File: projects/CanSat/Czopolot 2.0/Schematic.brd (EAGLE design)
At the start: 43 x 30.8 mm, 91 parts

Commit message: Work work..
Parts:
- removed U$13: DRV8833SOP, SobieskiSat2:SOP65P640X120-17T340X500N
- added C26: 10u, Unified:C0603
- added C27, C33: 100n, Unified:C0603
- added R18, R19: 100k, Unified:R0603
- added U$14, U$15: DRV8838, SobieskiSat2:SON50P200X200X80-9T90X160N
- BTN_DFU: value PUSH-SWITCH -> PUSH-SWITCHDIP; device SobieskiSat2:SWITCH_SMD -> SobieskiSat2:2X1_2.54
- C17: value 10u_pol -> 100n; device Unified:C1206 -> Unified:C0603
- C24: value 100n -> 10u
- C25: value 2.2u -> 100n
- R12: value 10k -> 100k
- moved D7 50.7 mm to (39.2, 25.8), turned to 90 degrees
- moved D8 48.4 mm to (39.2, 23.8), turned to 90 degrees
- moved D10 47.3 mm to (39.2, 17.8)
- moved D6 45.8 mm to (39.2, 27.8)
- moved R30 42.7 mm to (39.2, 16.0), turned to 180 degrees
- moved D2 41.7 mm to (39.2, 19.8)
- moved C21 41.0 mm to (8.25, 27.2), turned to 270 degrees
- moved D9 40.7 mm to (39.2, 21.8)
- moved R10 39.9 mm to (17.5, 28.0), turned to 90 degrees
- moved C23 39.8 mm to (9.50, 30.0), turned to 0 degrees
- moved C22 39.6 mm to (10.5, 27.2), turned to 90 degrees
- moved U$9 37.7 mm to (14.0, 28.2), turned to 90 degrees
- moved R14 34.8 mm to (25.5, 11.0)
- moved R15 33.3 mm to (21.0, 7.50), turned to 90 degrees
- moved D61 33.3 mm to (14.5, 3.75)
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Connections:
- removed net AIN1: U$13.16
- removed net AIN2: U$13.15
- removed net BIN1: U$13.9
- removed net BIN2: U$13.10
- removed net N$51: D10.A, R30.2
- new net EN_L: U$1.15, U$14.5
- new net EN_R: U$1.17, U$15.5
- new net N$32: D10.C, R30.1
- new net N$33: D61.1, R63.1, U$3.P$10
- new net N$34: MOTR.P$2, U$15.2
- new net N$36: MOTR.P$1, U$15.3
- new net N$39: C17.2, C24.2, U$15.8
- new net N$40: R19.1, U$15.7
- new net PH_L: U$1.14, U$14.6
- new net PH_R: U$1.16, U$15.6
- net DFU: no longer BTN_DFU.P$3
- net GND: now also C17.1, C24.1, C26.1, C27.1, C33.1, R30.2, U$14.4, U$14.9, U$15.4, U$15.9; no longer D10.C, U$13.13, U$13.17
- net GPS_RX: now also D61.2, U$1.29; no longer U$1.42, U$3.P$10
- net GPS_TX: now also R12.2, U$1.30; no longer R31.2, U$1.43
- net N$10: now also R5.1, U$10.7; no longer MOTL.P$2, U$13.2
- net N$15: now also RN1.1, U$1.38; no longer MOTR.P$1, U$13.5
- net N$19: now also RN1.2, U$1.37; no longer C17.1, C24.1, U$13.11
- net N$20: now also RN1.3, U$1.36; no longer D2.C, U$10.7
- net N$26: now also MOTL.P$1, U$14.3; no longer C25.2, U$13.14
- net N$28: now also RN1.4, U$1.35; no longer D2.A, R5.1
- net N$29: now also R31.2, U$1.43; no longer U$13.3
- net N$3: now also D2.C, R5.2; no longer MOTR.P$2, U$13.7
- net N$30: now also C25.2, C26.2, U$14.8; no longer U$13.6
- net N$31: now also R18.1, U$14.7; no longer R12.1, U$13.1
- net N$5: now also MOTL.P$2, U$14.2; no longer MOTL.P$1, U$13.4
- net SCL: now also R6.1, U$1.58; no longer R7.2, U$1.29
- net SDA: now also R7.1, U$1.59; no longer R6.2, U$1.30
- net VCC: now also D10.A, D2.A, R12.1, R18.2, R19.2, R6.2, R63.2, R7.2; no longer BTN_DFU.P$4, R12.2, R30.1, R5.2, R6.1, R7.1
- net VSYS: now also C27.2, C33.2, U$14.1, U$15.1; no longer C17.2, C24.2, U$13.12
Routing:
- net GND: track 84.0 -> 193.7 mm, vias 0 -> 8
- net VSYS: track 0.00 -> 54.0 mm
- net SCL: track 27.1 -> 0.00 mm, vias 1 -> 0
- net SDA: track 26.6 -> 0.00 mm, vias 1 -> 0
- net N$38: track 0.00 -> 22.2 mm, vias 0 -> 1
- net N$1: track 0.00 -> 21.4 mm, vias 0 -> 1
- net N$37: track 0.00 -> 21.0 mm, vias 0 -> 1
- net VCC: track 138.4 -> 117.7 mm, vias 3 -> 4
- net N$2: track 0.00 -> 20.0 mm, vias 0 -> 1
- net N$3: track 4.08 -> 23.8 mm, vias 0 -> 1
- net GPS_TX: track 23.2 -> 8.61 mm
- net PH_L: track 0.00 -> 14.4 mm
- net EN_L: track 0.00 -> 13.8 mm
- net USB_D-: track 17.9 -> 4.37 mm
- net USB_D+: track 17.0 -> 4.10 mm
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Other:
- board size 43 x 30.8 mm -> 44.2 x 30.8 mm
- board text removed: "^ Battery and switch holes or pads"

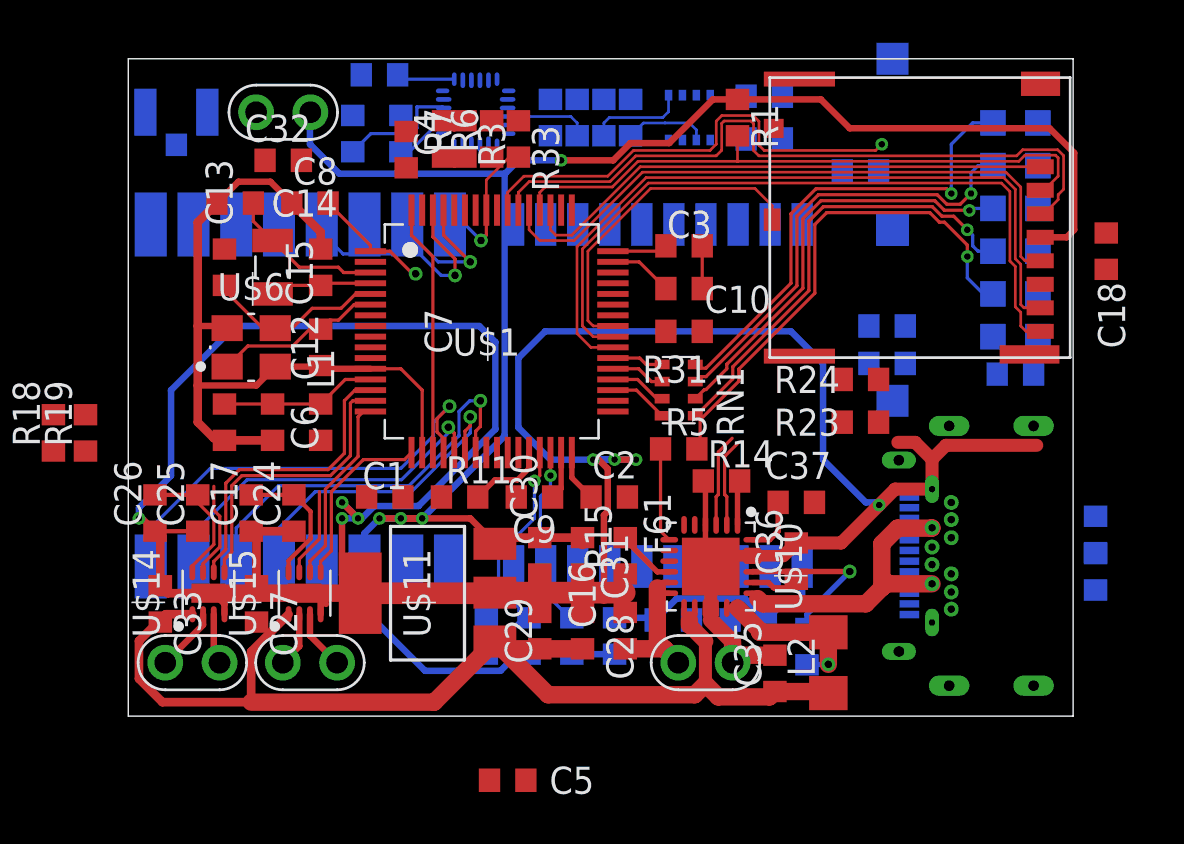
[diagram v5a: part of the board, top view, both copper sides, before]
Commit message: some 3D models added
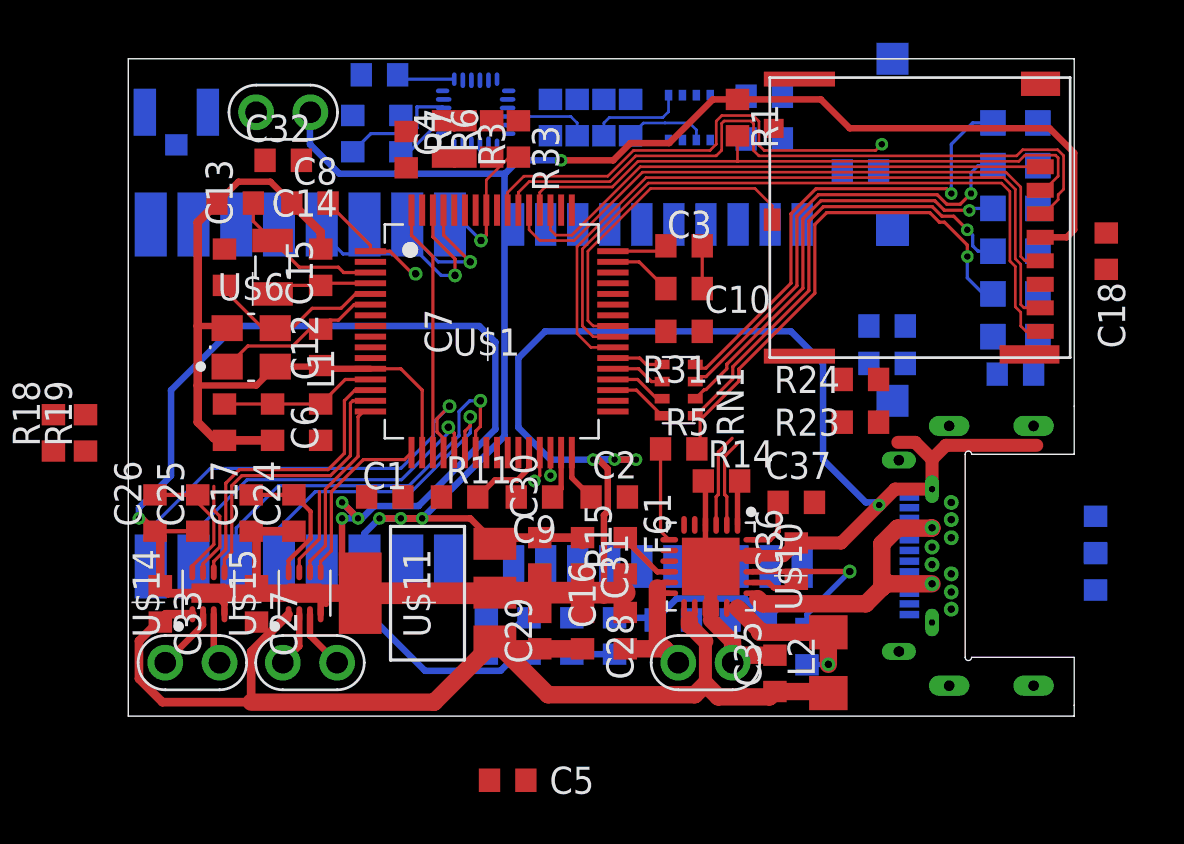
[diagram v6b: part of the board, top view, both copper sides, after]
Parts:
- U$12: device SobieskiSat2:CON_U.FL -> SobieskiSat2:GHI-CONNECTORS_U.FL-R-SMT-1
- U$3: value PA6H -> PA6H_
- turned U$12 to 0 degrees
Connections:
- net GND: now also U$12.GND1, U$12.GND2, U$3.12, U$3.19, U$3.3, U$3.8; no longer U$12.GND, U$12.GND@1, U$3.P$12, U$3.P$19, U$3.P$3, U$3.P$8
- net GPS_TX: now also U$3.9; no longer U$3.P$9
- net N$17: now also U$3.1; no longer U$3.P$1
- net N$33: now also U$3.10; no longer U$3.P$10
- net VBACKUP: now also U$3.4; no longer U$3.P$4
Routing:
- net GPS_RX: track 9.06 -> 1.43 mm
- net GPS_TX: track 8.61 -> 1.08 mm
- net N$33: track 5.40 -> 2.70 mm
- net N$17: track 11.5 -> 10.1 mm
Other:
- outline, holes or cut-outs redrawn

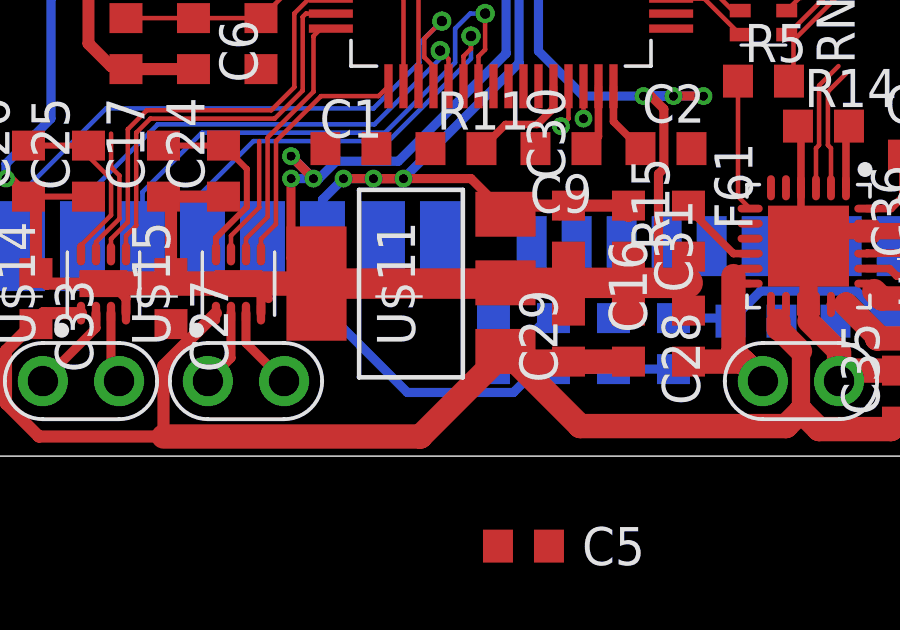
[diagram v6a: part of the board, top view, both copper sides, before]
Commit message: 3D Models added
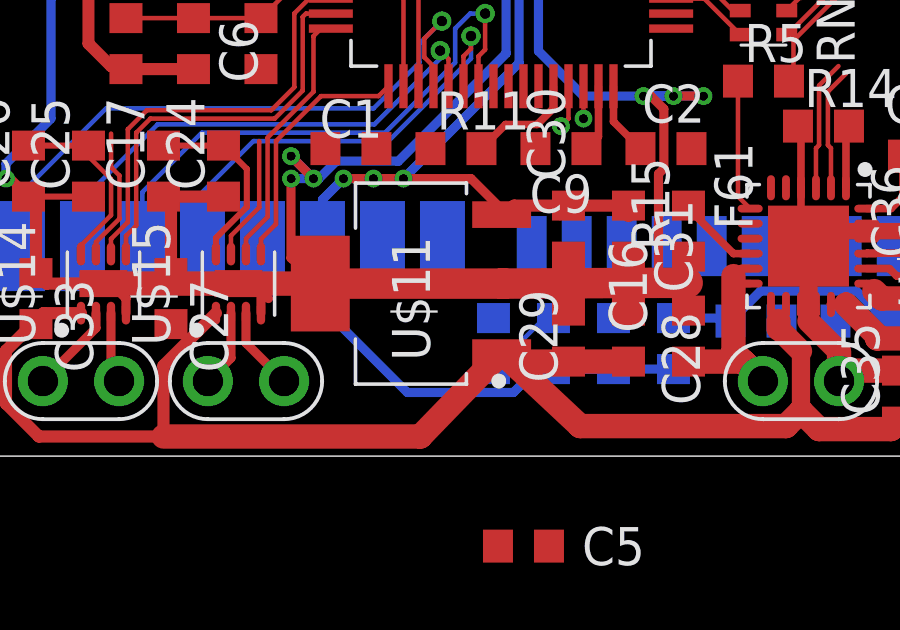
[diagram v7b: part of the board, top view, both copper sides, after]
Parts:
- U$11: device Unified:SOT223 -> Unified:SOT230P700X180-4N
- turned U$11 to 180 degrees

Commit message: Pheripherials added
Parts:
- added C38, C39: big_pol, Unified:C0603
- added U$13, U$16: SERVO, Unified:3X1_2.54
- added U$17, U$18, U$19, U$20, U$21, U$22, U$23, U$24, U$25, U$26, U$27, U$28: PAD, Unified:PAD
- moved RN1 28.0 mm to (51.5, 15.5), flipped to the bottom
- moved R5 23.2 mm to (45.8, 19.0), flipped to the bottom
- moved R18 20.3 mm to (11.0, 1.75), flipped to the bottom, turned to 180 degrees
- moved BTN_RST 18.6 mm to (52.0, 20.8)
- moved BTN_USR 18.3 mm to (51.2, 31.2)
- moved C11 18.0 mm to (40.5, 34.8)
- moved R19 18.0 mm to (11.0, 3.75), flipped to the bottom, turned to 180 degrees
- moved R2 17.8 mm to (40.5, 32.8)
- moved R30 17.4 mm to (44.0, 32.8)
- moved R24 9.85 mm to (23.0, 11.8), turned to 270 degrees
- moved R23 7.28 mm to (25.0, 11.8), turned to 270 degrees
- moved R3 6.29 mm to (13.2, 33.2)
- moved R33 6.29 mm to (16.8, 33.2)
- moved R6 6.29 mm to (15.5, 33.2)
- moved R7 6.29 mm to (14.2, 33.2)
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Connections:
- new net N$41: U$13.P$3
- new net N$42: U$16.P$3
- new net N$43: U$1.8, U$21.1
- new net N$44: U$1.9, U$22.1
- new net N$45: U$1.10, U$23.1
- new net N$46: U$1.11, U$24.1
- new net N$47: U$1.26, U$25.1
- new net N$48: U$1.27, U$26.1
- new net N$49: U$1.24, U$27.1
- new net N$50: U$1.25, U$28.1
- new net SWCLK: U$1.49, U$18.1
- new net SWDIO: U$1.46, U$17.1
- net GND: now also C38.1, C39.1, U$13.P$1, U$16.P$1, U$20.1
- net VCC: now also C38.2, C39.2, U$13.P$2, U$16.P$2, U$19.1
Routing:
- net GND: track 193.8 -> 106.6 mm, vias 8 -> 1
- net VCC: track 117.9 -> 57.9 mm, vias 4 -> 1
- net N$3: track 23.8 -> 0.00 mm, vias 1 -> 0
- net N$38: track 22.2 -> 0.00 mm, vias 1 -> 0
- net N$1: track 21.4 -> 0.00 mm, vias 1 -> 0
- net SWDIO: track 0.00 -> 21.3 mm
- net N$37: track 21.0 -> 0.00 mm, vias 1 -> 0
- net N$2: track 20.0 -> 0.00 mm, vias 1 -> 0
- net N$48: track 0.00 -> 19.0 mm, vias 0 -> 1
- net N$28: track 2.80 -> 21.8 mm, vias 0 -> 1
- net N$15: track 2.43 -> 21.2 mm, vias 0 -> 1
- net N$20: track 2.68 -> 21.4 mm, vias 0 -> 1
- net N$19: track 2.55 -> 21.1 mm, vias 0 -> 1
- net N$47: track 0.00 -> 17.5 mm, vias 0 -> 1
- net SWCLK: track 0.00 -> 17.1 mm
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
